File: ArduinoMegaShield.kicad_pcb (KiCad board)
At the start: 2 copper layers, 101.6 x 53.3 mm, 42 parts, among them J1 Power, J10 Conn_01x04_Socket, J11 Conn_01x02_Socket, J12 Conn_01x02_Socket, J13 Conn_01x02_Socket, J14 Conn_01x02_Socket, J15 Conn_01x04, J16 Conn_01x04, J17 Conn_01x10_Socket, J18 Barrel_Jack_Switch, J2 Analog, J3 Analog, J4 Digital, J5 PWM, J6 PWM, J7 Communication, J8 Conn_01x04_Socket, J9 Conn_01x04_Socket, Q1 IRLB8721PBF, Q2 IRLB8721PBF, Q3 IRLB8721PBF, Q4 IRLB8721PBF, Q5 IRLB8721PBF, Q6 IRLB8721PBF, Q7 IRLB8721PBF, U1 MP6500_Pololu, U2 MP6500_Pololu

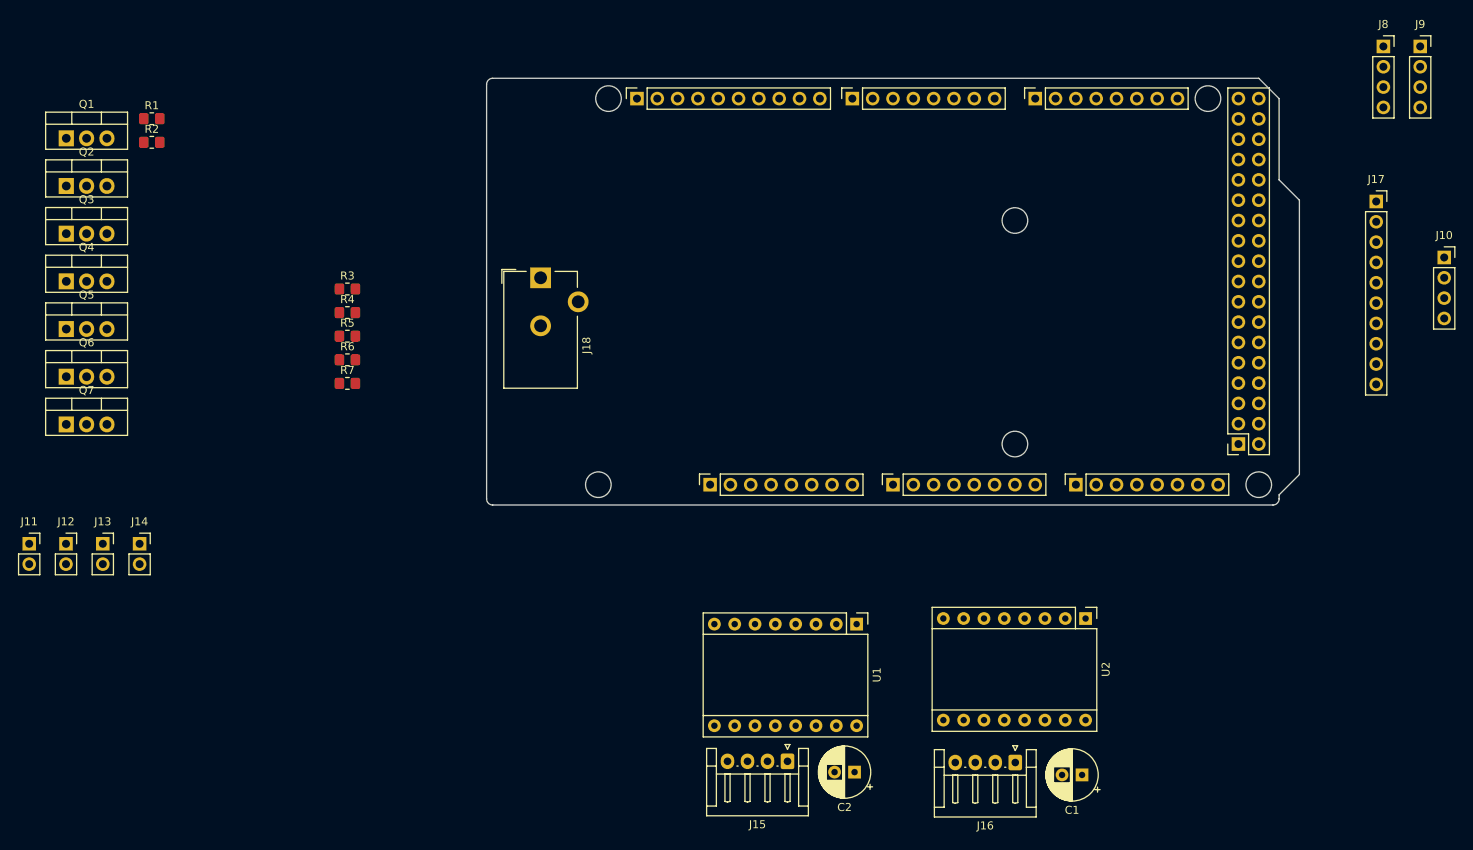
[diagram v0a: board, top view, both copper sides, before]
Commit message: Layout Placement done
-no fuse yet
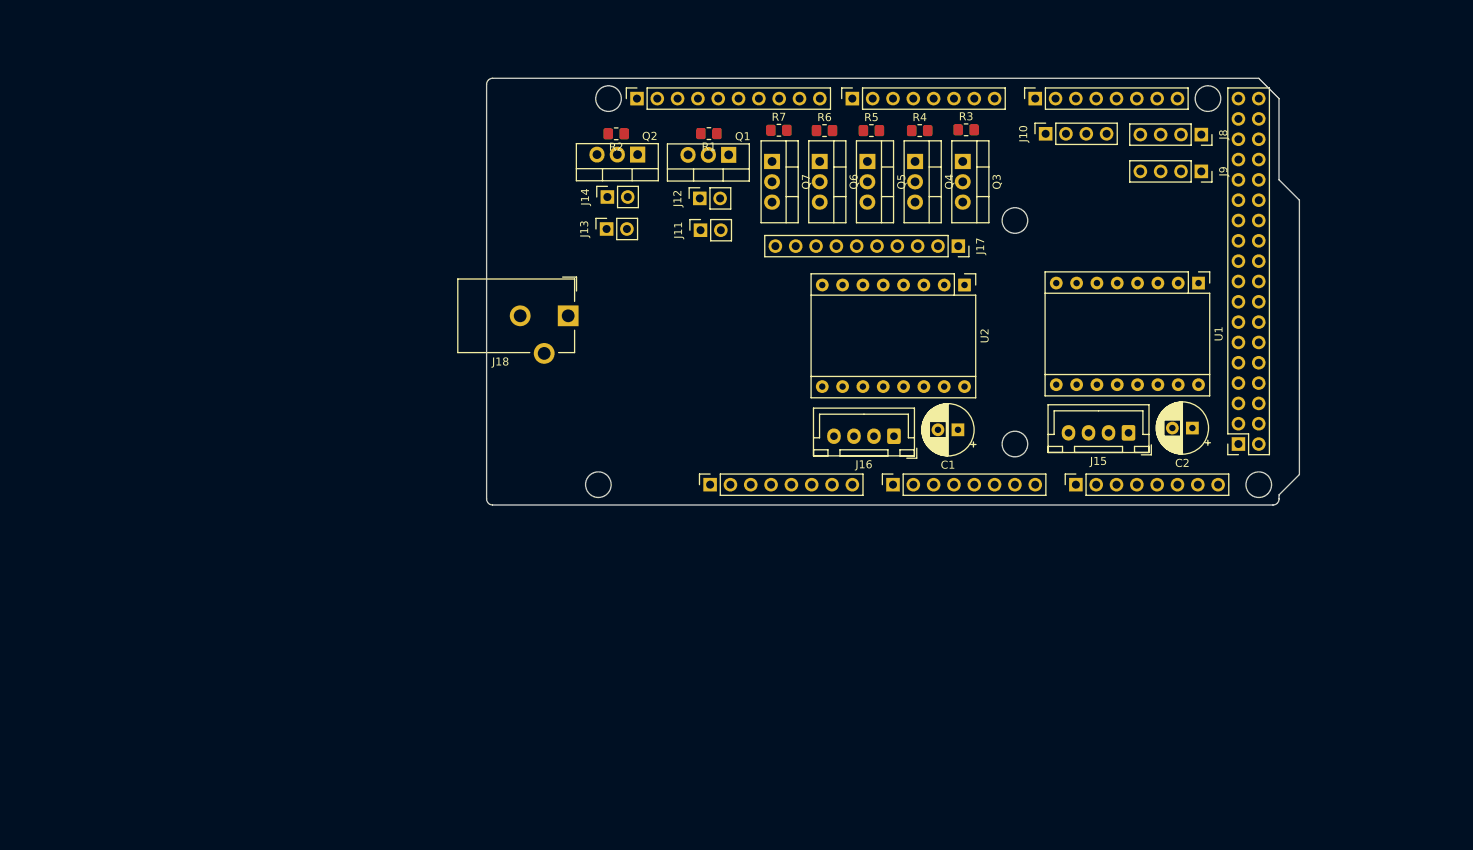
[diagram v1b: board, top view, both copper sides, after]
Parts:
- J15, J16: footprint Connector_JST:JST_EH_S4B-EH_1x04_P2.50mm_Horizontal -> Connector_JST:JST_XH_B4B-XH-A_1x04_P2.50mm_Vertical
- moved Q3 112.4 mm to (159.5, 57.1), turned to -90 degrees
- moved Q4 107.2 mm to (153.6, 57.1), turned to -90 degrees
- moved Q5 102.3 mm to (147.6, 57.1), turned to -90 degrees
- moved Q6 97.9 mm to (141.6, 57.1), turned to -90 degrees
- moved Q7 94.1 mm to (135.7, 57.1), turned to -90 degrees
- moved J11 92.6 mm to (126.7, 65.7), turned to 90 degrees
- moved J12 90.2 mm to (126.7, 61.7), turned to 90 degrees
- moved Q1 82.8 mm to (130.3, 56.2), turned to 180 degrees
- moved R3 79.9 mm to (159.9, 53.1)
- moved R4 75.1 mm to (154.1, 53.2)
- moved J13 74.3 mm to (115.0, 65.5), turned to 90 degrees
- moved J14 72.8 mm to (115.1, 61.5), turned to 90 degrees
- moved Q2 71.5 mm to (118.9, 56.2), turned to 180 degrees
- moved R5 70.4 mm to (148.1, 53.2)
- moved R1 69.7 mm to (127.8, 53.6), turned to 180 degrees
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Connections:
- U1 pad 1: unconnected-(U1-ENBL-Pad1) -> GND
- U2 pad 1: unconnected-(U2-ENBL-Pad1) -> GND

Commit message: Final Layout
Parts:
- removed the J13 at (115.0, 65.5)
- removed the J14 at (115.1, 61.5)
- removed J18: Barrel_Jack_Switch, Connector_BarrelJack:BarrelJack_CUI_PJ-102AH_Horizontal
- added F1: Fuse, Fuse:Fuseholder_TR5_Littelfuse_No560_No460, F.Cu at (102.6, 51.7)
- added J15: Conn_01x05_Socket, Connector_PinSocket_2.54mm:PinSocket_1x05_P2.54mm_Vertical, F.Cu at (184.5, 78.0)
- added J16: Conn_01x05_Socket, Connector_PinSocket_2.54mm:PinSocket_1x05_P2.54mm_Vertical, F.Cu at (189.2, 78.0)
- added SW1: 450301014042, footprints:SW_450301014042_WRE, F.Cu at (104.9, 83.0)
- J11, J12: value Conn_01x02_Socket -> Conn_01x03_Socket; footprint Connector_PinSocket_2.54mm:PinSocket_1x02_P2.54mm_Vertical -> Connector_PinSocket_2.54mm:PinSocket_1x03_P2.54mm_Vertical
- J17: value Conn_01x10_Socket -> L721RAHLP; footprint Connector_PinSocket_2.54mm:PinSocket_1x10_P2.54mm_Vertical -> L721RAHLP:SWITCHCRAFT_L721RAHLP
- moved J17 50.8 mm to (108.4, 73.0)
- moved J11 48.9 mm to (174.0, 77.9), turned to 0 degrees
- moved J12 45.8 mm to (169.5, 77.9), turned to 0 degrees
- moved J13 30.1 mm to (150.1, 91.6)
- moved U1 30.1 mm to (158.9, 73.1)
- moved C2 30.0 mm to (158.2, 91.0)
- moved U2 24.4 mm to (135.4, 73.2)
- moved J14 24.4 mm to (126.6, 91.7)
- moved C1 24.3 mm to (134.7, 91.1)
- moved J10 6.26 mm to (176.0, 54.9), turned to 0 degrees
- moved R2 6.13 mm to (122.3, 52.7), turned to 0 degrees
- moved J8 4.99 mm to (184.5, 54.9), turned to 0 degrees
- moved Q1 3.47 mm to (126.8, 56.7), turned to -90 degrees
- moved J9 3.40 mm to (189.0, 54.9), turned to 0 degrees
- moved Q6 2.89 mm to (138.8, 56.7)
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- renumbered J15 to J13, J16 to J14
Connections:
- J11 pad 1: +12V -> Net-(J11-Pin_1)
- J12 pad 2: Net-(J12-Pin_1) -> +12V
- J8 pad 1: VCC -> +5V
- J9 pad 1: VCC -> +5V
- Q1 pad 2: Net-(J12-Pin_1) -> Net-(J11-Pin_1)
- Q2 pad 2: Net-(J14-Pin_1) (its old number) -> Net-(J12-Pin_1)
- Q3 pad 2: Net-(J17-Pin_2) -> Net-(J15-Pin_1)
- Q4 pad 2: Net-(J17-Pin_4) -> Net-(J15-Pin_2)
- Q5 pad 2: Net-(J17-Pin_6) -> Net-(J15-Pin_3)
- Q6 pad 2: Net-(J17-Pin_8) -> Net-(J15-Pin_4)
- Q7 pad 2: Net-(J17-Pin_10) -> Net-(J15-Pin_5)
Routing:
- net +12V: track 0.00 -> 154.6 mm, vias 0 -> 1
- net +5V: track 0.00 -> 134.3 mm, vias 0 -> 2
- net /SCL/21: track 0.00 -> 97.1 mm
- net /SDA/20: track 0.00 -> 91.4 mm
- net Net-(J15-Pin_5): track 0.00 -> 72.0 mm
- net GND: track 0.00 -> 67.9 mm, vias 0 -> 30
- net Net-(J15-Pin_4): track 0.00 -> 61.9 mm
- net Net-(J12-Pin_1): track 0.00 -> 61.4 mm
- net Net-(J11-Pin_1): track 0.00 -> 59.0 mm
- net Net-(J15-Pin_3): track 0.00 -> 54.4 mm
- net /*4: track 0.00 -> 53.5 mm, vias 0 -> 1
- net /*5: track 0.00 -> 48.4 mm, vias 0 -> 1
- net Net-(J15-Pin_2): track 0.00 -> 46.7 mm
- net VCC: track 0.00 -> 45.4 mm
- net /*2: track 0.00 -> 40.4 mm, vias 0 -> 1
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- added copper zone on B.Cu, net GND
- added copper zone on F.Cu, net GND
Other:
- board text added: "*10"
- board text added: "*11"
- board text added: "*12"
- board text added: "*6"
- board text added: "*7"
- board text added: "*8"
- board text added: "*9"
- board text added: "12V"
- board text added: "5V"
- board text added: "5V Rail"
- board text added: "Designed and Built by Paul Tyagi Yihui Liang"
- board text added: "GND"
- board text added: "GPIO"
- board text added: "Heating Capacitors"
- board text added: "O2 Sensors"
- board text added: "Off"
- board text added: "On"
- board text added: "RX1"
- board text added: "SCL"
- board text added: "SDA"
- board text added: "TX1"
- board text added: "Temp Sensors"
- board text added: "Valves"

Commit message: fixed for DRC
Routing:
- net /*2: track 40.4 -> 35.2 mm, vias 1 -> 0
- net /*5: track 48.4 -> 46.5 mm, vias 1 -> 0
- net +12V: track 154.6 -> 153.3 mm, vias 1 -> 0
- net /SDA/20: track 91.4 -> 92.4 mm
- net +5V: track 134.3 -> 133.6 mm, vias 2 -> 0
- net GND: track 67.9 -> 68.0 mm, vias 30 -> 31
- net /*3: vias 1 -> 0
- net /*4: vias 1 -> 0
